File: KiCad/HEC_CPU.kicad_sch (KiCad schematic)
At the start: 10 parts, among them U1 Z80CPU, U12 74LS04, U16 74LS32, U18 74LS138, U20 74LS574, U21 74LS574, U22 74LS02, U23 74LS74, U6 74LS138, U7 28C256

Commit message: Complete fault generation circuit
Add circuit to generate fault on illegal IO access. The protection circuit design is not considered complete.
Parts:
- removed unit 4 of U22
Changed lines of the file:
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@@
-    )
-  )
-  (symbol (lib_id "74xx:74LS02") (at 58.42 171.45 0) (unit 4)
-    (in_bom yes) (on_board yes) (dnp no) (fields_autoplaced)
-    (property "Reference" "U22" (at 58.42 163.83 0)
-      (effects (font (size 1.27 1.27)))
-    )
-    (property "Value" "74LS02" (at 58.42 166.37 0)
-      (effects (font (size 1.27 1.27)))
-    )
-    (property "Footprint" "Package_DIP:DIP-14_W7.62mm_Socket" (at 58.42 171.45 0)
-      (effects (font (size 1.27 1.27)) hide)
-    )
-    (property "Datasheet" "http://www.ti.com/lit/gpn/sn74ls02" (at 58.42 171.45 0)
-      (effects (font (size 1.27 1.27)) hide)
-    )
-    (pin "1")
-    (pin "2")
-    (pin "3")
-    (pin "4")
-    (pin "5")
-    (pin "6")
-    (pin "10")
-    (pin "8")
-    (pin "9")
-    (pin "11")
-    (pin "12")
-    (pin "13")
-    (pin "14")
-    (pin "7")
-    (instances
-      (project "HEC1"
-        (path "/87935374-b60a-4f41-99da-94b76103dd77/73a0c68b-1e42-4c0d-ae31-b1a96d0648bb"
-          (reference "U22") (unit 4)
-        )
-      )
     )
   )

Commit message: Add HEC Bus
The HEC bus packs a lot of information into a small amount of pins. It is suitable for cards with various complexity.
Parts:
- added unit 1 of U22
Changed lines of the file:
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@@
     (effects (font (size 1.27 1.27)) (justify right))
   )
-  (hierarchical_label "D[0..7]" (shape output) (at 80.01 64.77 0) (fields_autoplaced)
+  (hierarchical_label "D[0..7]" (shape tri_state) (at 80.01 64.77 0) (fields_autoplaced)
     (effects (font (size 1.27 1.27)) (justify left))
   )
@@
     (effects (font (size 1.27 1.27)) (justify right))
   )
-  (hierarchical_label "~{NMI}" (shape output) (at 21.59 39.37 180) (fields_autoplaced)
+  (hierarchical_label "~{NMI}" (shape input) (at 21.59 39.37 180) (fields_autoplaced)
     (effects (font (size 1.27 1.27)) (justify right))
   )
@@
         )
       )
+    )
+  )
+  (symbol (lib_id "74xx:74LS02") (at 50.165 163.195 0) (unit 1)
+    (in_bom yes) (on_board yes) (dnp no) (fields_autoplaced)
+    (property "Reference" "U22" (at 50.165 154.94 0)
+      (effects (font (size 1.27 1.27)))
+    )
+    (property "Value" "74LS02" (at 50.165 157.48 0)
+      (effects (font (size 1.27 1.27)))
+    )
+    (property "Footprint" "" (at 50.165 163.195 0)
+      (effects (font (size 1.27 1.27)) hide)
+    )
+    (property "Datasheet" "http://www.ti.com/lit/gpn/sn74ls02" (at 50.165 163.195 0)
+      (effects (font (size 1.27 1.27)) hide)
+    )
+    (pin "1")
+    (pin "2")
+    (pin "3")
+    (pin "4")
+    (pin "5")
+    (pin "6")
+    (pin "10")
+    (pin "8")
+    (pin "9")
+    (pin "11")
+    (pin "12")
+    (pin "13")
+    (pin "14")
+    (pin "7")
+    (instances
+      (project "HEC1"
+        (path "/87935374-b60a-4f41-99da-94b76103dd77/73a0c68b-1e42-4c0d-ae31-b1a96d0648bb"
+          (reference "U22") (unit 1)
+        )
+      )

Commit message: Created footprint for HEC bus
Created footprints for HEC bus and some other updates.
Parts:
- U18: footprint (none) -> Package_DIP:DIP-16_W7.62mm_Socket
- U22: footprint (none) -> Package_DIP:DIP-14_W7.62mm_Socket
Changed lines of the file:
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@@
       (effects (font (size 1.27 1.27)))
     )
-    (property "Footprint" "" (at 50.165 163.195 0)
+    (property "Footprint" "Package_DIP:DIP-14_W7.62mm_Socket" (at 50.165 163.195 0)
       (effects (font (size 1.27 1.27)) hide)
     )
@@
       (effects (font (size 1.27 1.27)) (justify left))
     )
-    (property "Footprint" "" (at 36.83 125.73 0)
-      (effects (font (size 1.27 1.27)) hide)
-    )
+    (property "Footprint" "Package_DIP:DIP-16_W7.62mm_Socket" (at 36.83 125.73 0)
+      (effects (font (size 1.27 1.27)) hide)
+    )

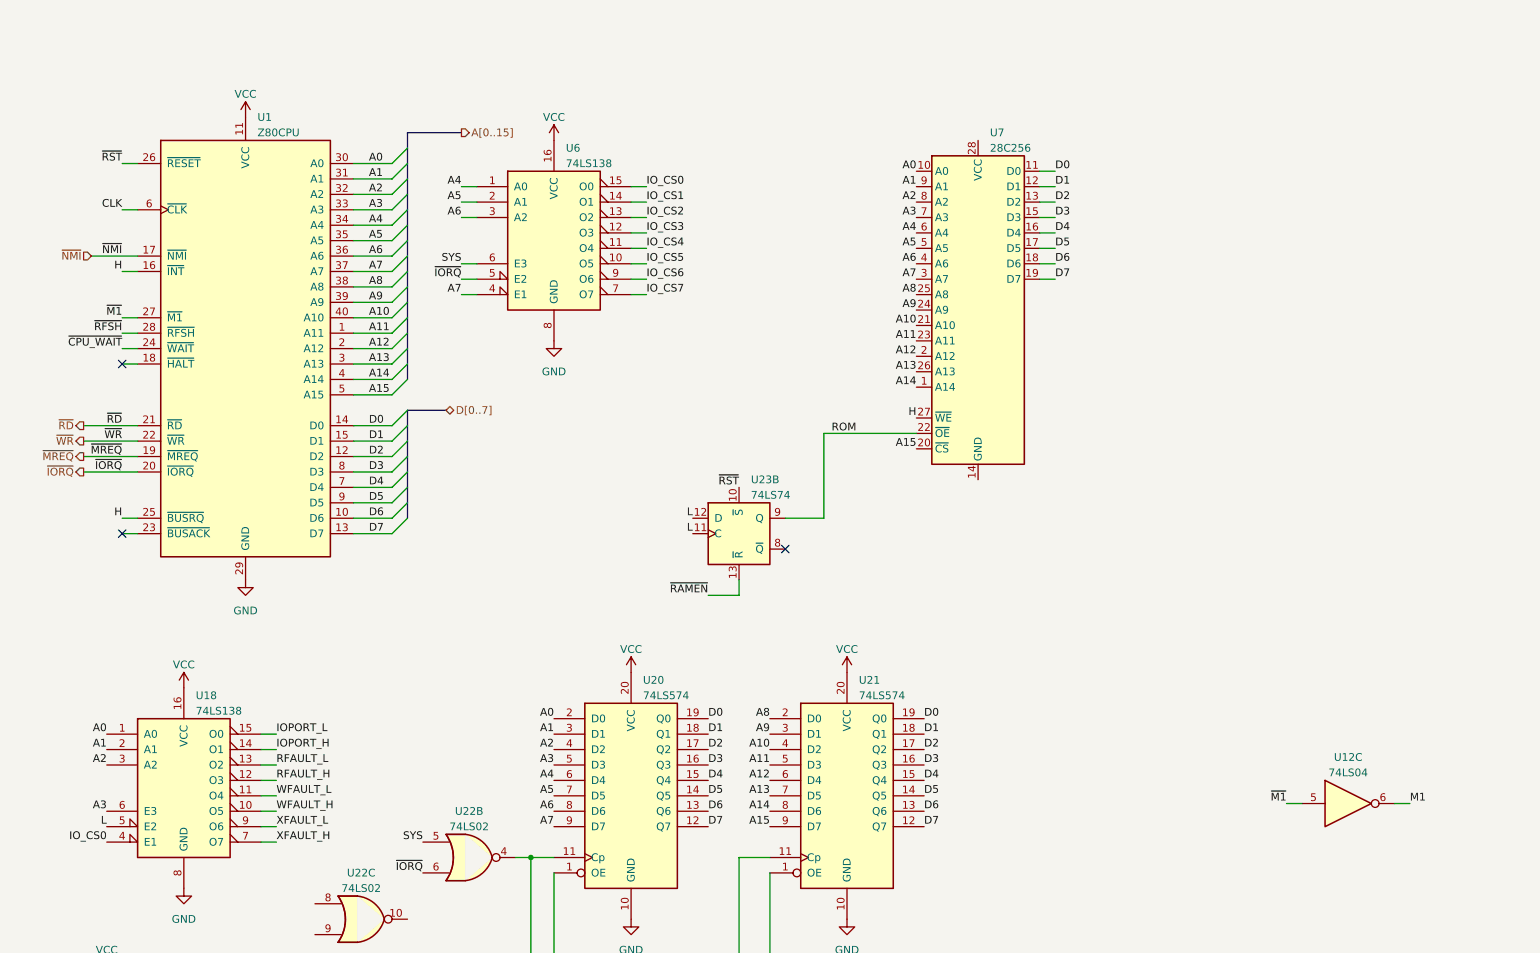
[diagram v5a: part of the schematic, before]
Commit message: IO implementation
Implemented most of IO functions, add connections between the schematics.
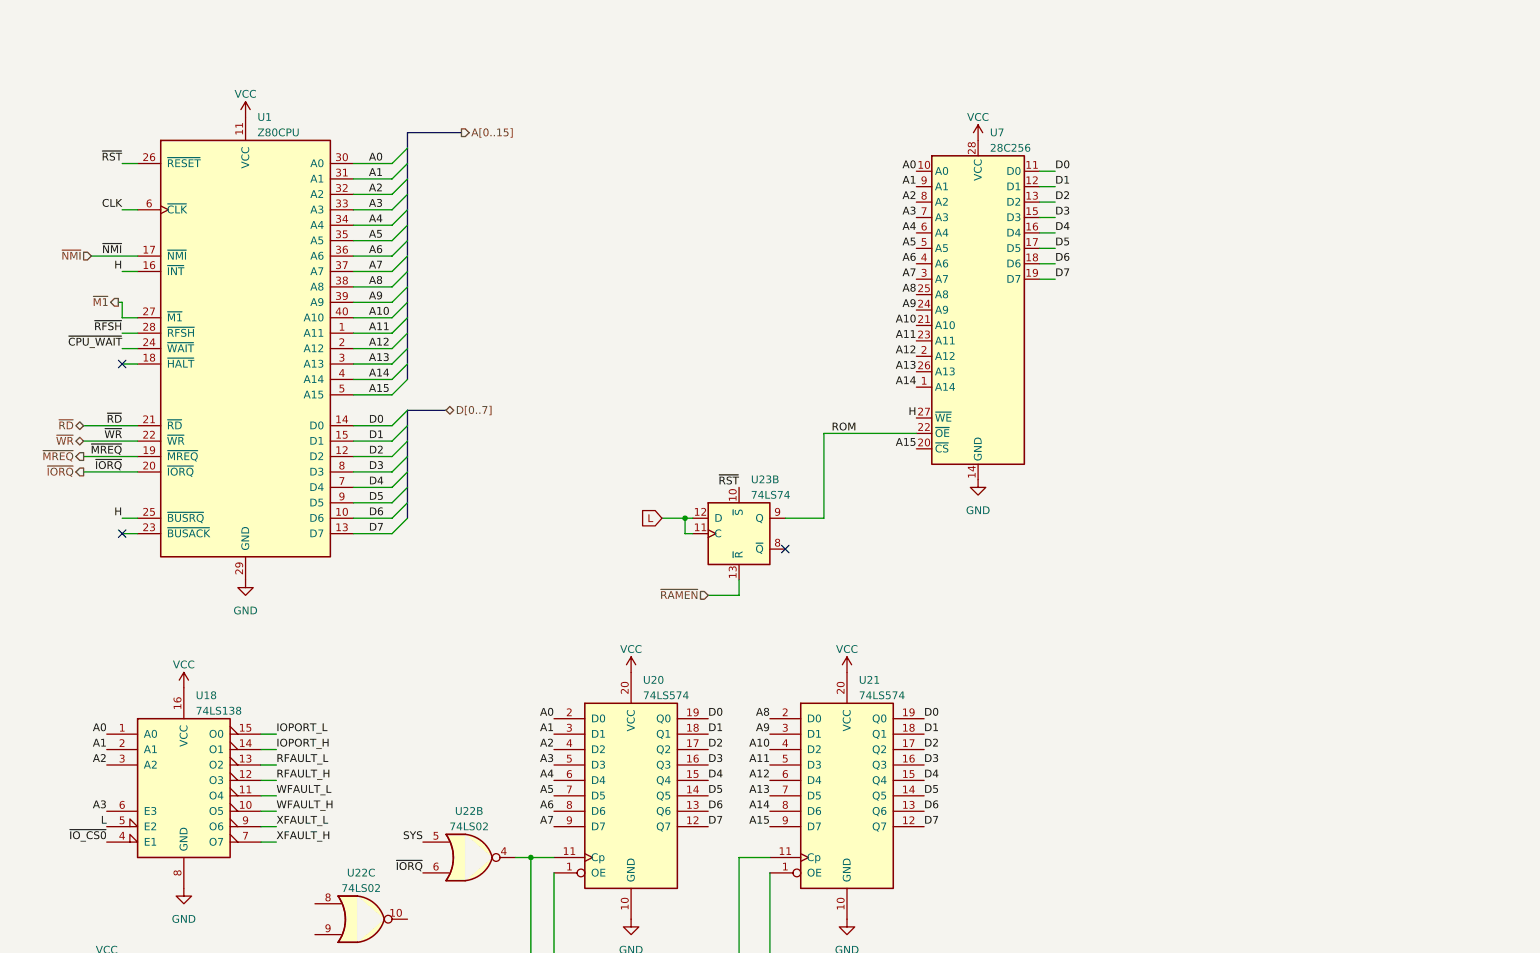
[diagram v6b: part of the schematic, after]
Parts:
- removed unit 3 of U12
- removed U6: 74LS138, Package_DIP:DIP-16_W7.62mm_Socket, symbol 74xx:74LS138
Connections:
- net GND: now also U7.14 (GND)
- net VCC: now also U7.28 (VCC)
- net IO_CS0 renamed ~{IO_CS0}

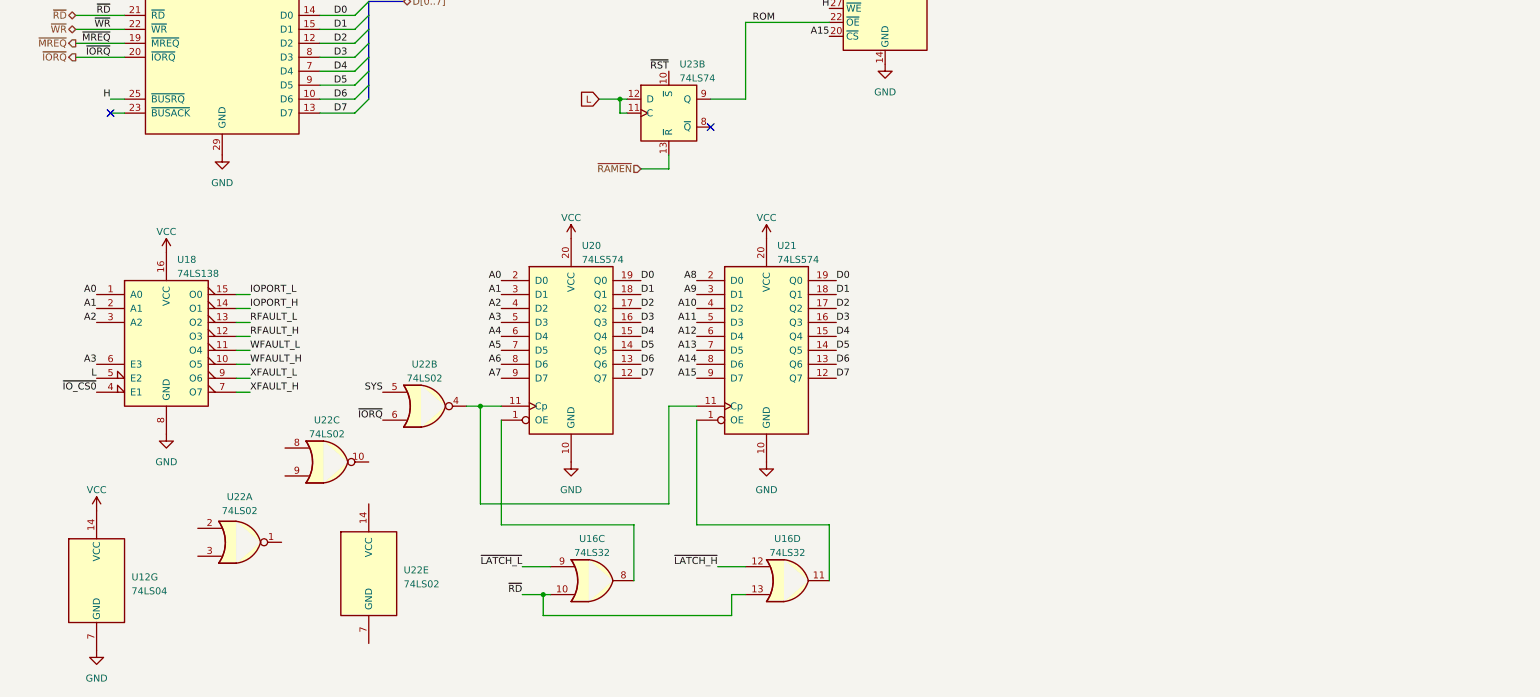
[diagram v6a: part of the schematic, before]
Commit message: Add wait state generator
Add circuit to generate 0 to 15 wait states or use external wait input.
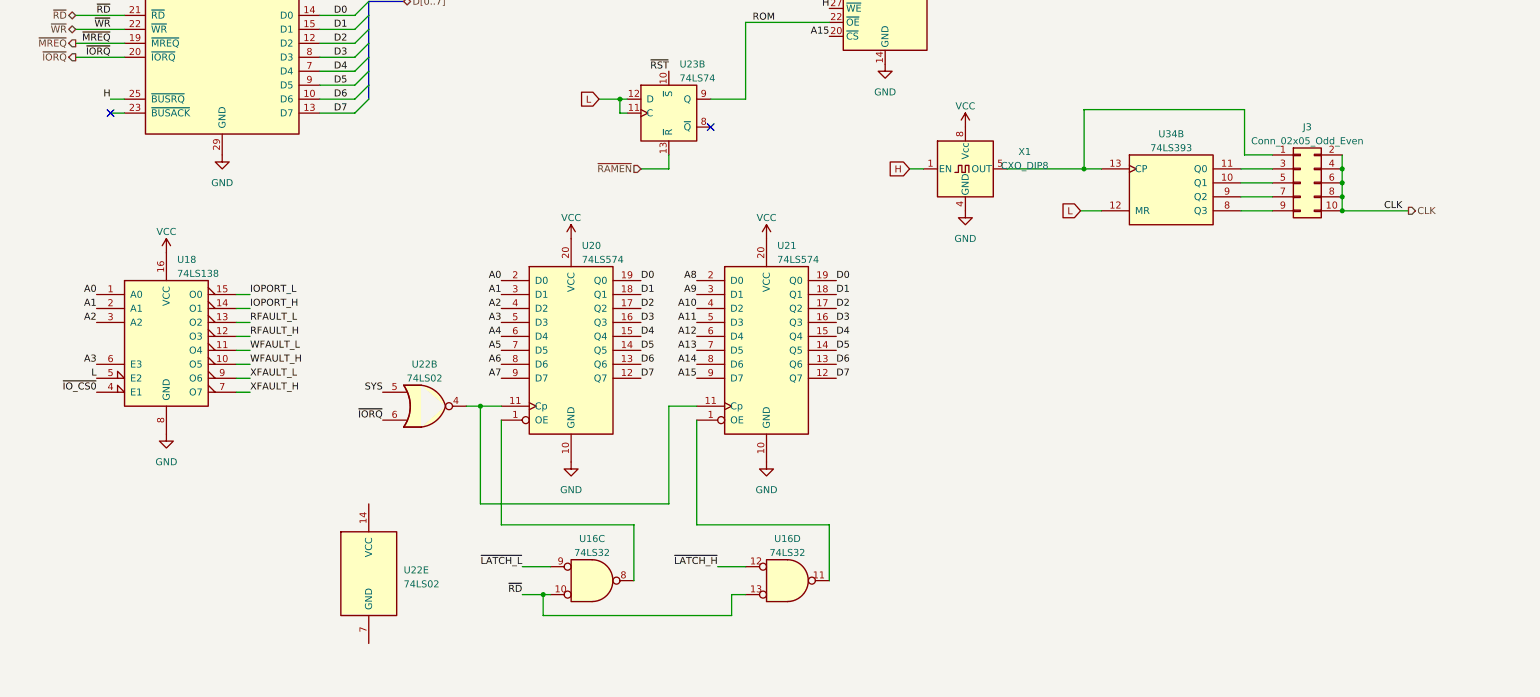
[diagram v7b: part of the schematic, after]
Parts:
- removed U12: 74LS04, Package_DIP:DIP-14_W7.62mm_Socket, symbol 74xx:74LS04
- removed unit 1 of U22
- removed unit 3 of U22
- added J3: Conn_02x05_Odd_Even, symbol Connector_Generic:Conn_02x05_Odd_Even
- added U34: 74LS393, symbol 74xx:74LS393
- added X1: CXO_DIP8, Oscillator:Oscillator_DIP-8, symbol Oscillator:CXO_DIP8
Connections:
- net CLK: now also J3.10 (Pin_10), J3.2 (Pin_2), J3.4 (Pin_4), J3.6 (Pin_6), J3.8 (Pin_8)
- net GND: now also X1.4 (GND)
- net H: now also X1.1 (EN)
- net L: now also U34.12 (MR)
- net VCC: now also X1.8 (Vcc)
- new net: J3.5 (Pin_5), U34.10 (Q1)
- new net: J3.3 (Pin_3), U34.11 (Q0)
- new net: J3.1 (Pin_1), U34.13 (CP), X1.5 (OUT)
- new net: J3.9 (Pin_9), U34.8 (Q3)
- new net: J3.7 (Pin_7), U34.9 (Q2)

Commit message: MATX-compliant motherboard
Made the motherboard mounting holes and card positions MATX compliant. The MATX motherboard edge is shifted 0.5 inches to the left, which is annoying. Also, cards have component on the opposite side from ISA, meaning PCI slot positioning must be followed. However, PCI pins are not 0.1inch apart, so lining up is tricky. I don't know whether I got it right.
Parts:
- J3: footprint (none) -> Connector_PinHeader_2.54mm:PinHeader_2x05_P2.54mm_Vertical
- U34: footprint (none) -> Package_DIP:DIP-14_W7.62mm_Socket
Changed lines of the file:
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@@
       (effects (font (size 1.27 1.27)))
     )
-    (property "Footprint" "" (at 219.71 97.79 0)
+    (property "Footprint" "Package_DIP:DIP-14_W7.62mm_Socket" (at 219.71 97.79 0)
       (effects (font (size 1.27 1.27)) hide)
     )
@@
       (effects (font (size 1.27 1.27)))
     )
-    (property "Footprint" "" (at 243.205 97.79 0)
-      (effects (font (size 1.27 1.27)) hide)
-    )
+    (property "Footprint" "Connector_PinHeader_2.54mm:PinHeader_2x05_P2.54mm_Vertical" (at 243.205 97.79 0)
+      (effects (font (size 1.27 1.27)) hide)
+    )
